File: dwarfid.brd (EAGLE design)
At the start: 48.9 x 36.9 mm, 17 parts, among them Q1 mmbt3904, Q4 mmbt3906, Q5 mmbt3906

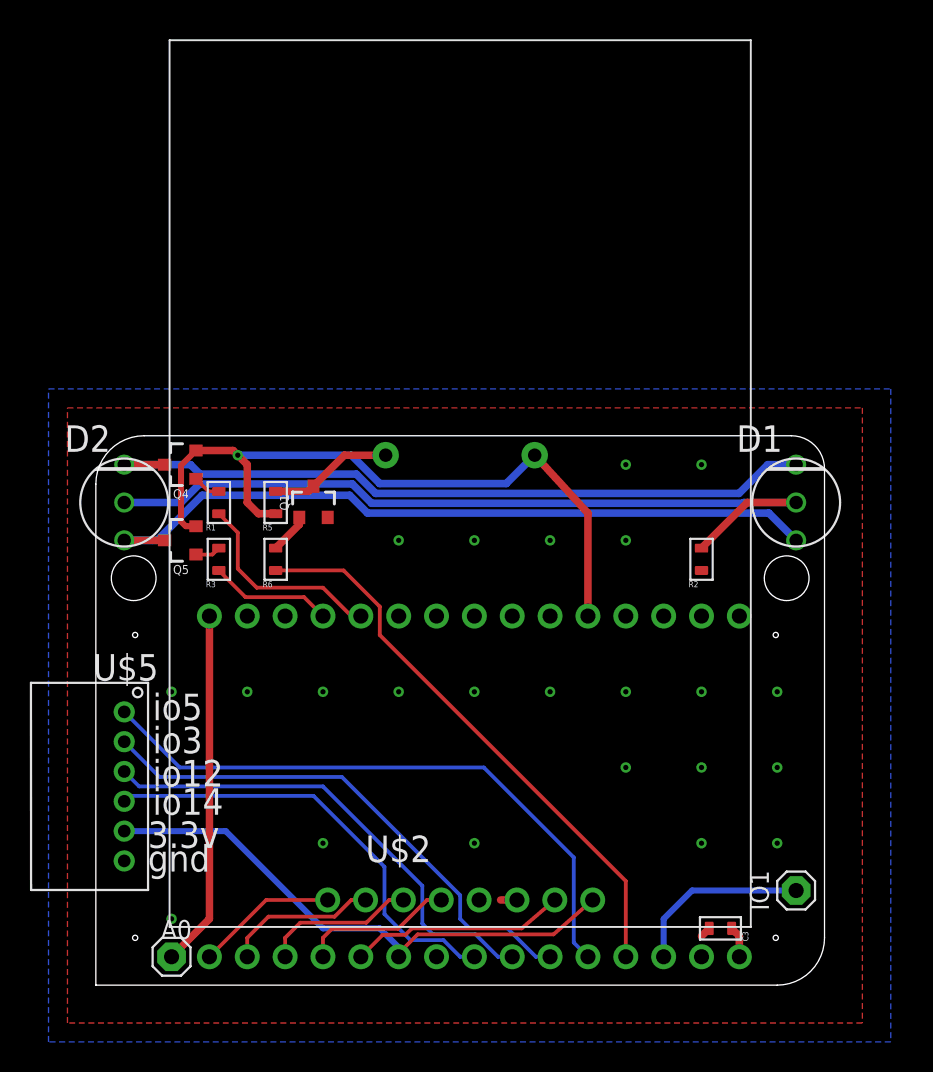
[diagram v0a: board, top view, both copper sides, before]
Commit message: fixed the spacing for the nodeMCU pins
moved the LEDs to the bottom of the display

Changed the current setting resistor for both the LEDs and the buzzer to 100 ohms.

remapped the rfid card reader to use pins that can also be used as hardware spi pins.

Put both the buzzer and the LEDs on pwm compatible pins

replaced the 6pin jst connector with an 8pin connector.

added the other hardware spi pins to the jst connector.
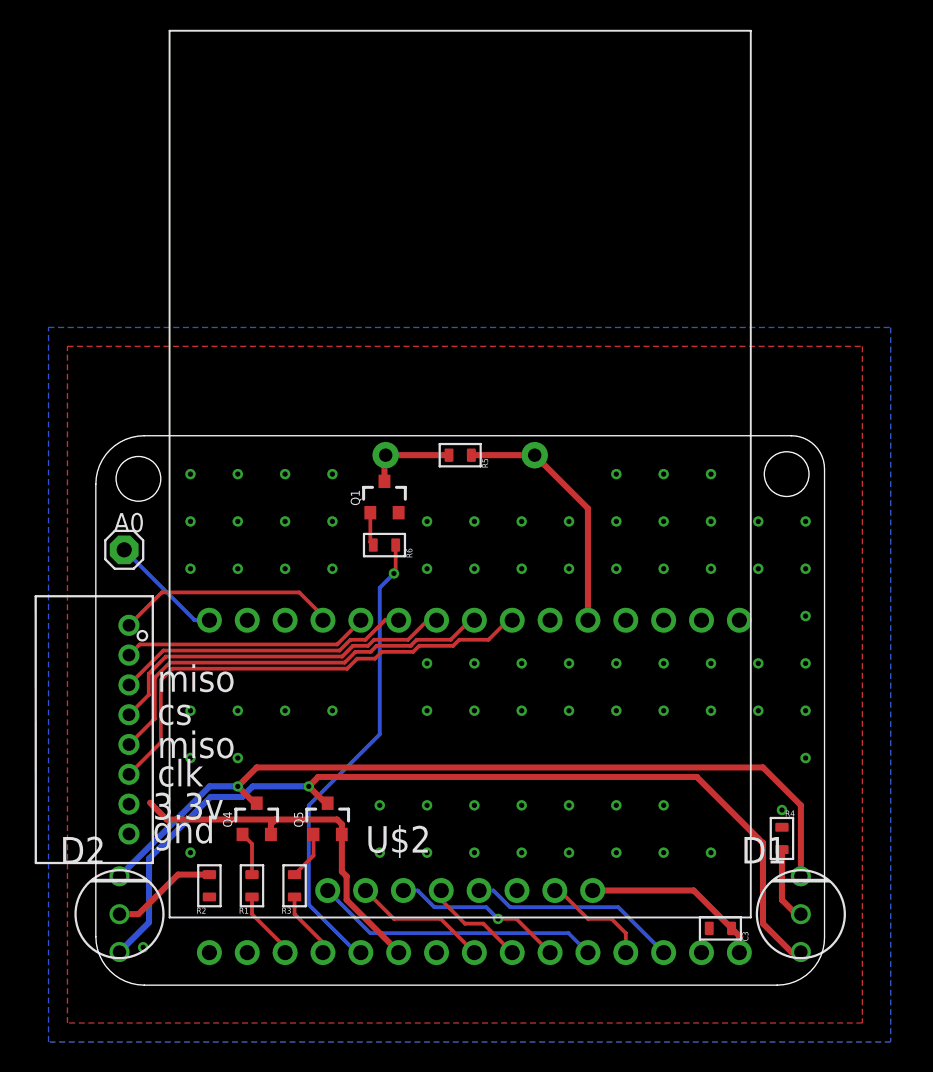
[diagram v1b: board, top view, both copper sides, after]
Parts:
- removed IO1: (no value), adafruit:1X01
- removed U$5: JST6_2MM_RIGHTANGLE, rowe_connectors:JST_2MM_6POS
- added R4: 100, rowe_passives:PASSIVE_0603
- added U$3: JST8_2MM_RIGHTANGLE, rowe_connectors:JST_2MM_8POS
- R2: value 28 -> 100
- R5: value (none) -> 100
- R6: value (none) -> 1k
- moved R2 39.6 mm to (7.62, 7.30)
- moved D1 27.6 mm to (47.3, 5.40)
- moved D2 27.6 mm to (1.59, 5.40)
- moved A0 27.5 mm to (1.91, 29.8)
- moved R1 25.8 mm to (10.5, 7.30)
- moved Q4 24.3 mm to (10.8, 11.7), turned to 0 degrees
- moved R3 22.5 mm to (13.3, 7.30)
- moved Q5 21.2 mm to (15.6, 11.7), turned to 0 degrees
- moved R5 12.8 mm to (24.4, 36.2), turned to 0 degrees
- moved R6 7.36 mm to (19.4, 30.2), turned to 0 degrees
- moved Q1 4.77 mm to (19.4, 33.3)
- moved U$2 0.63 mm to (24.4, 34.9)
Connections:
- removed net IO_OUT1: U$1.D5, U$5.4
- removed net IO_OUT2: U$1.D6, U$5.3
- removed net IO_OUT3: U$1.D7, U$5.2
- removed net IO_OUT4: U$1.D8, U$5.1
- removed net N$10: IO1.1, U$1.D10
- removed net N$7: U$2.5
- new net CLK: U$1.CLK, U$3.6
- new net CS: U$1.CMD, U$3.4
- new net IO10_OUT: U$1.SD3, U$3.1
- new net IO9_OUT: U$1.SD2, U$3.2
- new net MISO: U$1.SD0, U$3.5
- new net MOSI: U$1.SD1, U$3.3
- new net N$11: D1.2, R4.P$1
- new net N$12: U$1.D1
- new net N$13: U$1.D0
- new net RFID_IRQ: U$1.D10, U$2.5
- net 3.3V: now also U$3.7; no longer U$5.5
- net BUZZER: now also U$1.D4; no longer U$1.D9
- net GND: now also R4.P$2, U$3.8; no longer U$5.6
- net G_LED: now also U$1.D3; no longer U$1.SD3
- net N$1: no longer D1.2
- net RFID_CS: now also U$1.D8; no longer U$1.D0
- net RFID_MISO: now also U$1.D6; no longer U$1.D3
- net RFID_MOSI: now also U$1.D7; no longer U$1.D2
- net RFID_RST: now also U$1.D9; no longer U$1.D4
- net RFID_SCK: now also U$1.D5; no longer U$1.D1
- net R_LED: now also U$1.D2; no longer U$1.SD2
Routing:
- net N$1: track 53.8 -> 7.13 mm
- net IO_OUT4: track 41.3 -> 0.00 mm
- net IO_OUT3: track 35.5 -> 0.00 mm
- net 3.3V: track 88.0 -> 53.8 mm, vias 1 -> 0
- net IO_OUT2: track 32.7 -> 0.00 mm
- net CLK: track 0.00 -> 32.5 mm
- net IO_OUT1: track 30.0 -> 0.00 mm
- net MISO: track 0.00 -> 28.2 mm
- net CS: track 0.00 -> 24.1 mm
- net MOSI: track 0.00 -> 19.9 mm
- net IO9_OUT: track 0.00 -> 16.5 mm
- net N$8: track 23.9 -> 7.67 mm
- net IO10_OUT: track 0.00 -> 14.9 mm
- net RFID_IRQ: track 0.00 -> 14.1 mm
- net N$10: track 12.2 -> 0.00 mm
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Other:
- outline, holes or cut-outs redrawn
- board text added: "clk"
- board text added: "cs"
- board text added: "miso"
- board text removed: "io12"
- board text removed: "io14"
- board text removed: "io3"
- board text removed: "io5"

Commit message: minor intermediate changed before switching out the LEDs for
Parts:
- R5: value 100 -> 1k
- R6: value 1k -> 100
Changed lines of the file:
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@@
 <attribute name="PROD_ID" value="TRANS-08049" x="19.3675" y="33.3375" size="1.778" layer="27" display="off"/>
 </element>
-<element name="R5" library="rowe_passives" library_urn="urn:adsk.eagle:library:487190" package="PASSIVE_0603" package3d_urn="urn:adsk.eagle:package:487200/4" value="100" x="24.4475" y="36.195"/>
-<element name="R6" library="rowe_passives" library_urn="urn:adsk.eagle:library:487190" package="PASSIVE_0603" package3d_urn="urn:adsk.eagle:package:487200/4" value="1k" x="19.3675" y="30.1625"/>
+<element name="R5" library="rowe_passives" library_urn="urn:adsk.eagle:library:487190" package="PASSIVE_0603" package3d_urn="urn:adsk.eagle:package:487200/4" value="1k" x="24.4475" y="36.195"/>
+<element name="R6" library="rowe_passives" library_urn="urn:adsk.eagle:library:487190" package="PASSIVE_0603" package3d_urn="urn:adsk.eagle:package:487200/4" value="100" x="19.3675" y="30.1625"/>
 <element name="U$2" library="controller_boards" library_urn="urn:adsk.eagle:library:486412" package="RC522" package3d_urn="urn:adsk.eagle:package:486418/3" value="RC522" x="24.4475" y="34.925" smashed="yes">
 <attribute name="NAME" x="18.0975" y="9.525" size="1.778" layer="25"/>

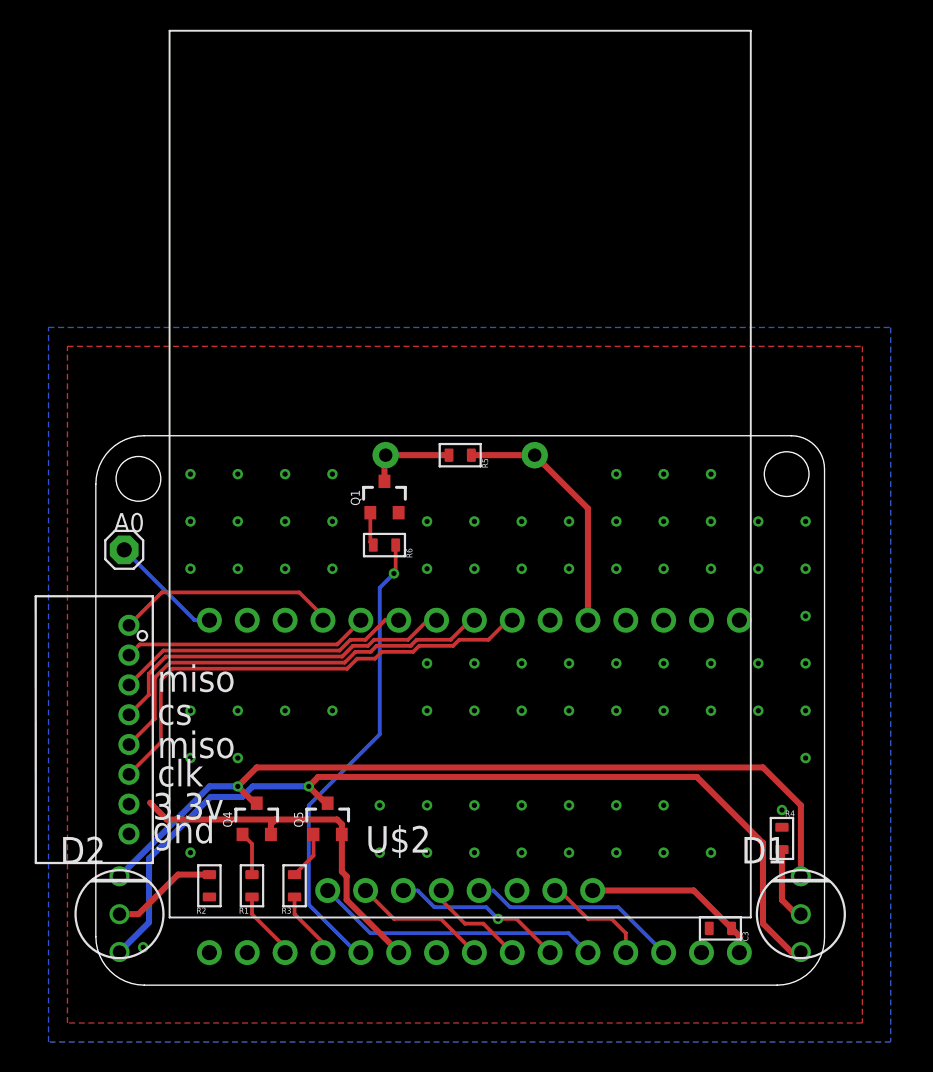
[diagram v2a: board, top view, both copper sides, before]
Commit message: replaced the LEDs with WS2812Bs.
Moved the rfid board down so that it will be easier to solder.

unfortunately both of these changes required us to increase the size of the board.
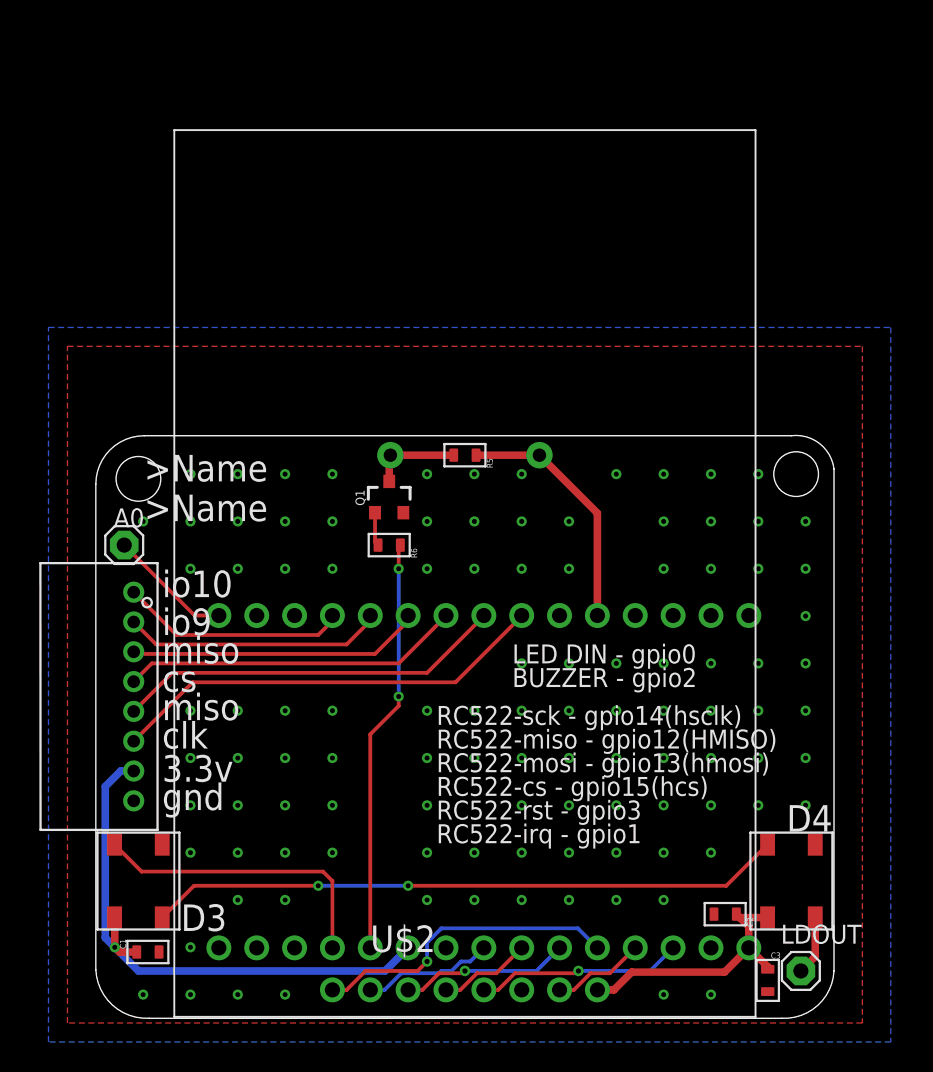
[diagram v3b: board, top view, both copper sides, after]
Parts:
- removed D1, D2: (no value), rowe_actuators:LED_3_PIN_THROUGHHOLE
- removed Q4, Q5: mmbt3906, SparkFun-DiscreteSemi:SOT23-3
- removed R1, R3: 1k, rowe_passives:PASSIVE_0603
- removed R2, R4: 100, rowe_passives:PASSIVE_0603
- added C1, C2: 100nf, rowe_passives:PASSIVE_0603
- added D3, D4: WS2812B, rowe_actuators:WS2812B
- added LDOUT: (no value), adafruit:1X01
- moved U$2 6.68 mm to (24.8, 28.3)
- moved C3 4.72 mm to (45.1, 0.95), turned to 90 degrees
- moved U$3 2.25 mm to (2.54, 20.0)
- moved U$1 0.71 mm to (24.8, 14.3)
- moved A0 0.32 mm to (1.91, 30.2)
- moved B1 0.32 mm to (24.8, 36.2)
- moved Q1 0.32 mm to (19.7, 33.3)
- moved R5 0.32 mm to (24.8, 36.2)
- moved R6 0.32 mm to (19.7, 30.2)
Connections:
- removed net G_LED: R3.P$2, U$1.D3
- removed net N$1: D2.2, R2.P$1
- removed net N$11: D1.2, R4.P$1
- removed net N$12: U$1.D1
- removed net N$13: U$1.D0
- removed net N$3: D1.1, D2.1, Q4.3
- removed net N$4: Q5.1, R3.P$1
- removed net N$5: D1.P$3, D2.P$3, Q5.3
- removed net R_LED: R1.P$2, U$1.D2
- new net LIGHT_DIN: D3.P$4, U$1.D3
- new net N$7: D3.P$2, D4.P$4
- net 3.3V: now also C1.P$2, C2.P$2, D3.P$1, D4.P$1; no longer Q4.2, Q5.2
- net GND: now also C1.P$1, C2.P$1, D3.P$3, D4.P$3; no longer R2.P$2, R4.P$2
- net N$2: now also D4.P$2, LDOUT.1; no longer Q4.1, R1.P$1
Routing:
- net N$5: track 62.9 -> 0.00 mm, vias 1 -> 0
- net N$3: track 56.3 -> 0.00 mm, vias 1 -> 0
- net N$7: track 0.00 -> 42.9 mm, vias 0 -> 2
- net LIGHT_DIN: track 0.00 -> 20.1 mm
- net 3.3V: track 53.8 -> 72.4 mm, vias 0 -> 1
- net N$1: track 7.13 -> 0.00 mm
- net N$11: track 5.04 -> 0.00 mm
- net R_LED: track 4.65 -> 0.00 mm
- net G_LED: track 4.52 -> 0.00 mm
- net BUZZER: track 31.4 -> 27.9 mm, vias 1 -> 2
- net N$4: track 3.22 -> 0.00 mm
- net CLK: track 32.5 -> 29.6 mm
- net MISO: track 28.2 -> 26.2 mm
- net RFID_CS: track 19.2 -> 20.8 mm, vias 0 -> 1
- net IO9_OUT: track 16.5 -> 18.0 mm
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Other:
- board size 48.9 x 36.9 mm -> 49.5 x 39.1 mm
- board text added: "BUZZER - gpio2"
- board text added: "LED DIN - gpio0"
- board text added: "RC522-cs - gpio15(hcs)"
- board text added: "RC522-irq - gpio1"
- board text added: "RC522-miso - gpio12(HMISO)"
- board text added: "RC522-mosi - gpio13(hmosi)"
- board text added: "RC522-rst - gpio3"
- board text added: "RC522-sck - gpio14(hsclk)"
- board text added: "io10"
- board text added: "io9"

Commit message: Moved the board up so that the bottom line is at y=0
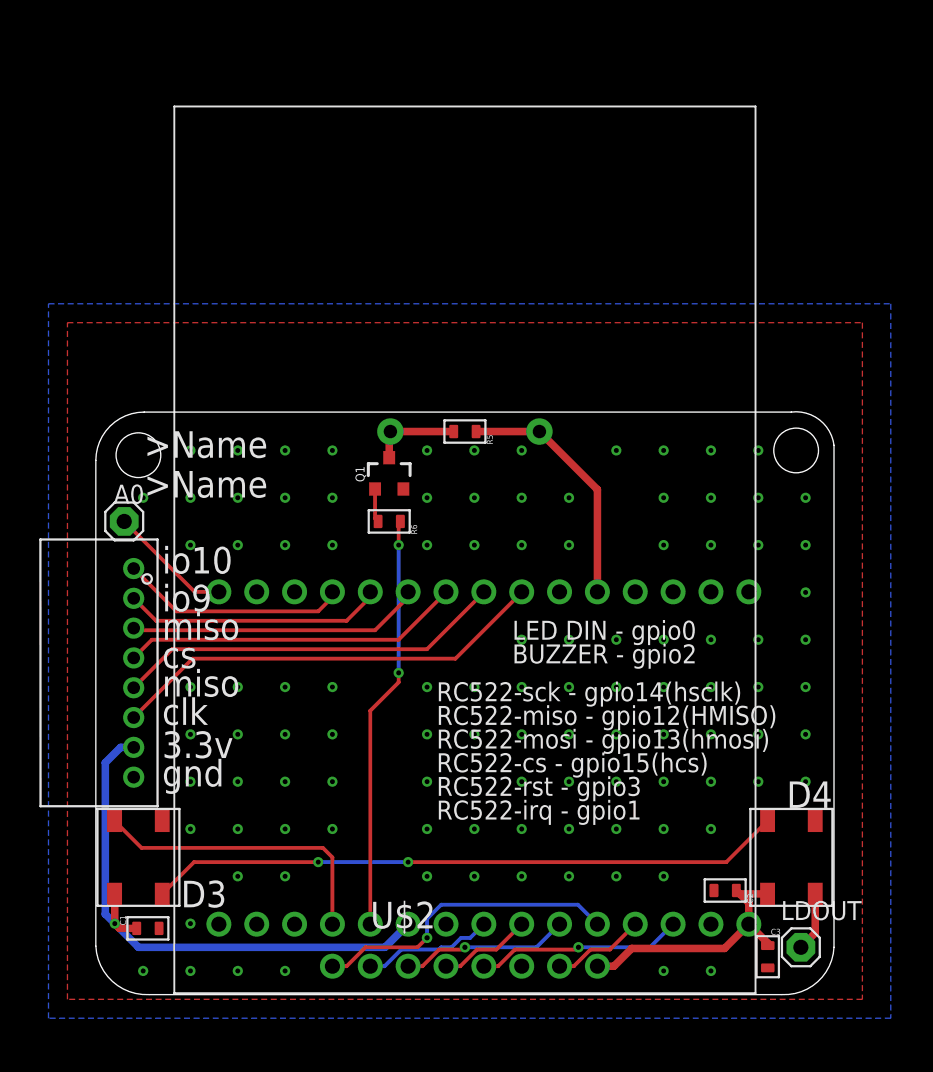
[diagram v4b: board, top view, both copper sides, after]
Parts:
- moved C1 1.59 mm to (3.49, 4.45)
- moved C2 1.59 mm to (42.2, 6.99)
- moved U$1 1.59 mm to (24.8, 15.9)
- moved C3 1.59 mm to (45.1, 2.54)
- moved LDOUT 1.59 mm to (47.3, 3.17)
- moved D3 1.59 mm to (2.86, 9.21)
- moved D4 1.59 mm to (46.7, 9.21)
- moved A0 1.59 mm to (1.91, 31.8)
- moved B1 1.59 mm to (24.8, 37.8)
- moved Q1 1.59 mm to (19.7, 34.9)
- moved R5 1.59 mm to (24.8, 37.8)
- moved R6 1.59 mm to (19.7, 31.8)
- moved U$2 1.59 mm to (24.8, 29.8)
- moved U$3 1.59 mm to (2.54, 21.6)
